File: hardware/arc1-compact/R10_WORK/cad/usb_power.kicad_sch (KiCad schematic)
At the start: 19 parts, among them J1 USB-C receptacle, U1 TUSB320LAI, U2 TPD2EUSB30

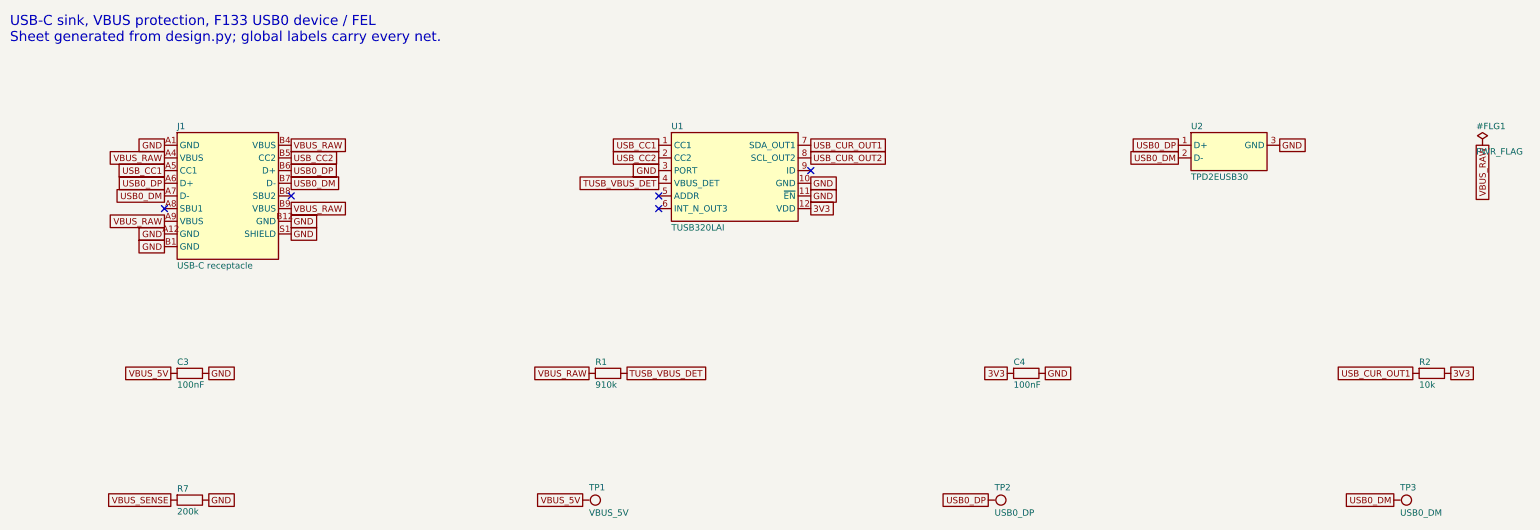
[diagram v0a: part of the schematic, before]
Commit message: R10 change order rev 1.1: HDMI audio (ADV7513), USB0 role mux + hub + 2x front USB-A, eMMC, buttonless board
Owner handoff ARC1_R10_Handoff rev 1.1 (spec/, SHA-256 recorded) implemented in the generated schematic:
- D8 ADV7513BSWZ replaces the TFP410 (supersedes D6): D213 RGB888 video, D213 I2C2 init,
  F133 I2S2 -> HDMI embedded audio; own 1.8 V buck + 3 filtered domains; R_EXT 887R.
  D[23:0] pin order verified from the datasheet glyph coordinates.
- D9 F133 USB0 -> TS3USB221A (default rear USB-C device/FEL) or USB2422 hub -> two
  TPS2051C-switched front USB-A ports; F133 USB1 remains the internal D213 link; the D213
  recovery USB-C becomes internal fixture pads.
- D10 Samsung KLMAG1JETD-B041 16 GB eMMC on F133 SMHC0 (CONDITIONAL: SMHC0 documented for SD).
- D11 no switches: fixture pad pairs; game buttons, microSD and speakers removed.
- crosscheck_r10 section I (handoff go/no-go: 4 exterior connectors, 0 switches, I2S wired
  to the HDMI transmitter, USB0/USB1 roles, eMMC wiring) PASS; ERC 0/0; pin review PASS.
Sources: ADV7513 DS Rev B (LCSC copy), ADI AN-1270, Linux adv7511 driver, USB2422
DS00001726A, TPS20xxC SLVSAU6I, Samsung eMMC DS (not committed: vendor-confidential mark).

Co-Authored-By: Claude Opus 5.5 <noreply@anthropic.com>
Claude-Session: https://claude.ai/code/session_01UkiuLdbjDvK75uDzAPKsGs
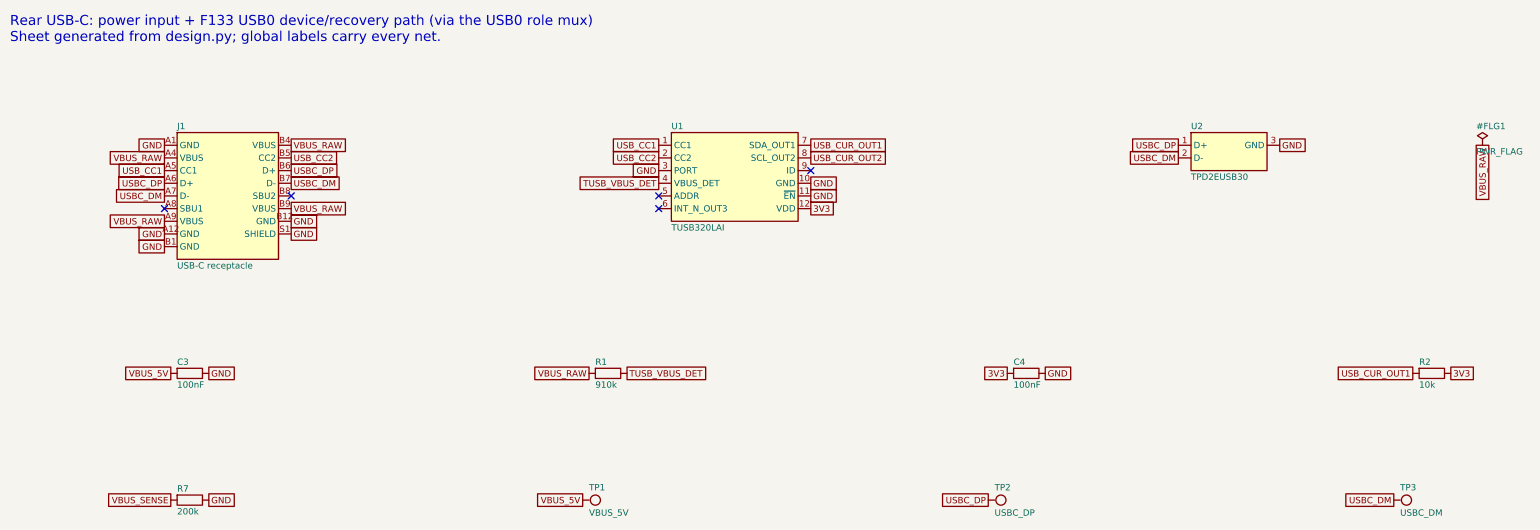
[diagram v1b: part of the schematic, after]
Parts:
- J1: Note power input + F133 USB0 (console / FEL); sink only -> REAR. Power input (auto-start, no switch) + F133 USB0 devic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
- TP2: value USB0_DP -> USBC_DP
- TP3: value USB0_DM -> USBC_DM
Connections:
- net USB0_DM renamed USBC_DM
- net USB0_DP renamed USBC_DP
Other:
- note added: "Rear USB-C: power input + F133 USB0 device/recovery path (via the USB0 role mux) Sheet generated from design.py; global labels carry every net."
- note removed: "USB-C sink, VBUS protection, F133 USB0 device / FEL Sheet generated from design.py; global labels carry every net."
- title: ARC-1 Compact R10: USB-C sink, VBUS protection, F133 USB0 device / FEL -> ARC-1 Compact R10: Rear USB-C: power input + F133 USB0 device/recovery path (via the USB0 role mux)
